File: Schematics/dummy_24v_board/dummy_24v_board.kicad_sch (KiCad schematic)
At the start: 2 parts, among them J1 Stack Male Edge Connector, J2 Conn_01x02_Socket

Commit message: Board setup with footprint
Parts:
- J2: footprint (none) -> footprints:CONN_2-1445057-2_TYCO
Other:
- moved on the sheet: J2
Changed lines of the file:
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@@
 	(symbol
 		(lib_id "Connector:Conn_01x02_Socket")
-		(at 90.17 62.23 0)
+		(at 85.09 71.12 0)
 		(unit 1)
 		(exclude_from_sim no)
@@
 		(on_board yes)
 		(dnp no)
-		(fields_autoplaced yes)
 		(property "Reference" "J2"
-			(at 91.44 62.2299 0)
+			(at 86.36 71.1199 0)
 			(effects
 				(font
@@
 		)
 		(property "Value" "Conn_01x02_Socket"
-			(at 91.44 64.7699 0)
+			(at 86.36 73.6599 0)
 			(effects
 				(font
@@
 			)
 		)
-		(property "Footprint" ""
-			(at 90.17 62.23 0)
+		(property "Footprint" "footprints:CONN_2-1445057-2_TYCO"
+			(at 89.154 64.516 0)
 			(effects
 				(font
 					(size 1.27 1.27)
 				)
-				(hide yes)
 			)
 		)
 		(property "Datasheet" "~"
-			(at 90.17 62.23 0)
+			(at 85.09 71.12 0)
 			(effects
 				(font
@@
 		)
 		(property "Description" "Generic connector, single row, 01x02, script generated"
-			(at 90.17 62.23 0)
+			(at 85.09 71.12 0)
 			(effects
 				(font

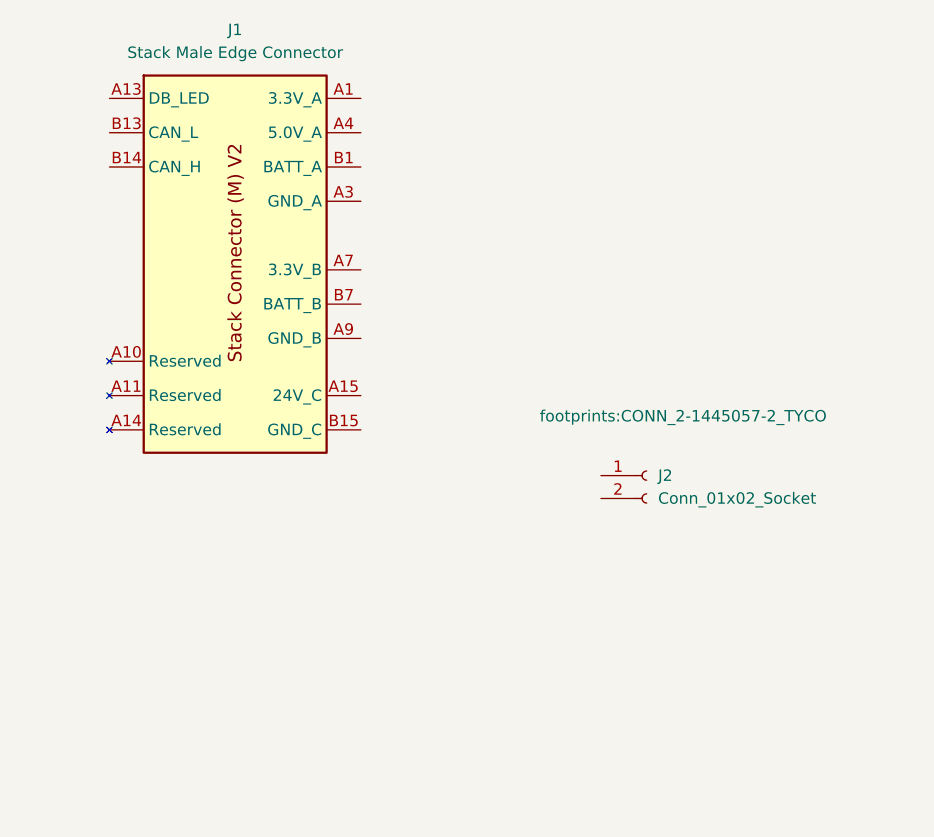
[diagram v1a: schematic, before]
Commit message: added two TestPoints for BATT 1&2
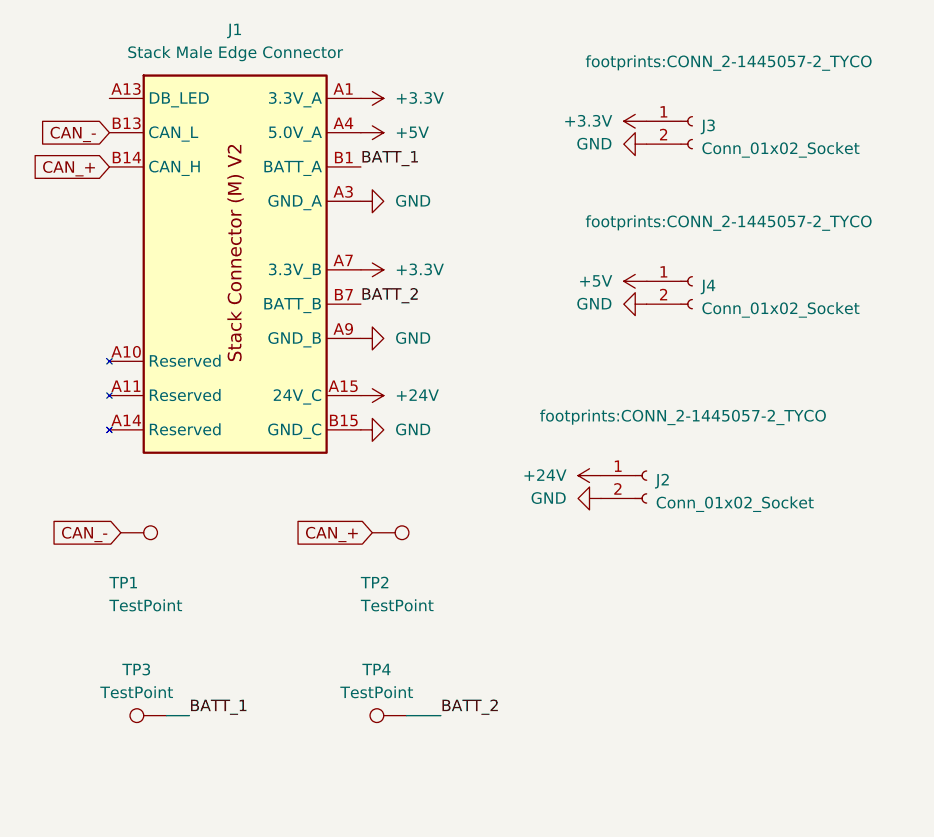
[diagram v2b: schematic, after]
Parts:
- added J3, J4: Conn_01x02_Socket, footprints:CONN_2-1445057-2_TYCO, symbol Connector:Conn_01x02_Socket
- added TP1, TP2, TP3, TP4: TestPoint, TestPoint:TestPoint_Pad_2.0x2.0mm, symbol Connector:TestPoint
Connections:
- net +3.3V: now reaches J1.A1 (3.3V_A), J1.A2 (3.3V_A)
- net +3.3V: now also J1.A7 (3.3V_B), J1.A8 (3.3V_B), J3.1 (Pin_1)
- net GND: now reaches J1.A12 (GND_B), J1.A9 (GND_B), J1.B10 (GND_B), J1.B11 (GND_B), J1.B12 (GND_B)
- net GND: now also J1.A3 (GND_A), J1.A6 (GND_A), J1.B15 (GND_C), J1.B16 (GND_C), J1.B17 (GND_C), J1.B18 (GND_C), J1.B4 (GND_A), J1.B5 (GND_A), J1.B6 (GND_A), J2.2 (Pin_2), J3.2 (Pin_2), J4.2 (Pin_2)
- net +24V: now reaches J1.A15 (24V_C), J1.A16 (24V_C), J1.A17 (24V_C), J1.A18 (24V_C)
- net +24V: now also J2.1 (Pin_1)
- net BATT_1: now reaches J1.B1 (BATT_A), J1.B2 (BATT_A), J1.B3 (BATT_A)
- net BATT_1: now also TP3.1
- net CAN_-: now reaches J1.B13 (CAN_L)
- net CAN_-: now also TP1.1
- net CAN_+: now reaches J1.B14 (CAN_H)
- net CAN_+: now also TP2.1
- net BATT_2: now reaches J1.B7 (BATT_B), J1.B8 (BATT_B), J1.B9 (BATT_B)
- net BATT_2: now also TP4.1
- net 5.0V_A renamed +5V
- net +5V: now also J4.1 (Pin_1)

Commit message: Connectors model added
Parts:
- J2, J3, J4: DIgiKey (none) -> 2-1445057-2
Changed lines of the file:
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@@
+			)
+		)
+		(property "DIgiKey" "2-1445057-2"
+			(at 90.17 31.75 0)
+			(effects
+				(font
+					(size 1.27 1.27)
+				)
+				(hide yes)
 			)
 		)
@@
 			)
 		)
+		(property "DIgiKey" "2-1445057-2"
+			(at 90.17 49.53 0)
+			(effects
+				(font
+					(size 1.27 1.27)
+				)
+				(hide yes)
+			)
+		)
 		(pin "2"
 		)
@@
 			)
 		)
+		(property "DIgiKey" ""
+			(at 39.37 48.26 0)
+			(effects
+				(font
+					(size 1.27 1.27)
+				)
+				(hide yes)
+			)
+		)
 		(pin "B6"
 		)
@@
 			)
 		)
+		(property "DIgiKey" ""
+			(at 54.61 77.47 0)
+			(effects
+				(font
+					(size 1.27 1.27)
+				)
+				(hide yes)
+			)
+		)
 		(pin "1"
 		)
@@
 			)
 		)
+		(property "DIgiKey" "2-1445057-2"
+			(at 85.09 71.12 0)
+			(effects
+				(font
+					(size 1.27 1.27)
+				)
+				(hide yes)
+			)
+		)
 		(pin "2"
 		)
@@
 		)
 		(property "Description" "test point"
+			(at 26.67 77.47 0)
+			(effects
+				(font
+					(size 1.27 1.27)
+				)
+				(hide yes)
+			)
+		)
+		(property "DIgiKey" ""
 			(at 26.67 77.47 0)
 			(effects
@@
 			)
 		)
+		(property "DIgiKey" ""
+			(at 58.42 97.79 0)
+			(effects
+				(font
+					(size 1.27 1.27)
+				)
+				(hide yes)
+			)
+		)
 		(pin "1"
 		)
@@
 			(at 31.75 97.79 0)
 			(effects
+				(font
+					(size 1.27 1.27)
+				)
+				(hide yes)
+			)
+		)
+		(property "DIgiKey" ""
+			(at 31.75 97.79 0)
+			(effects

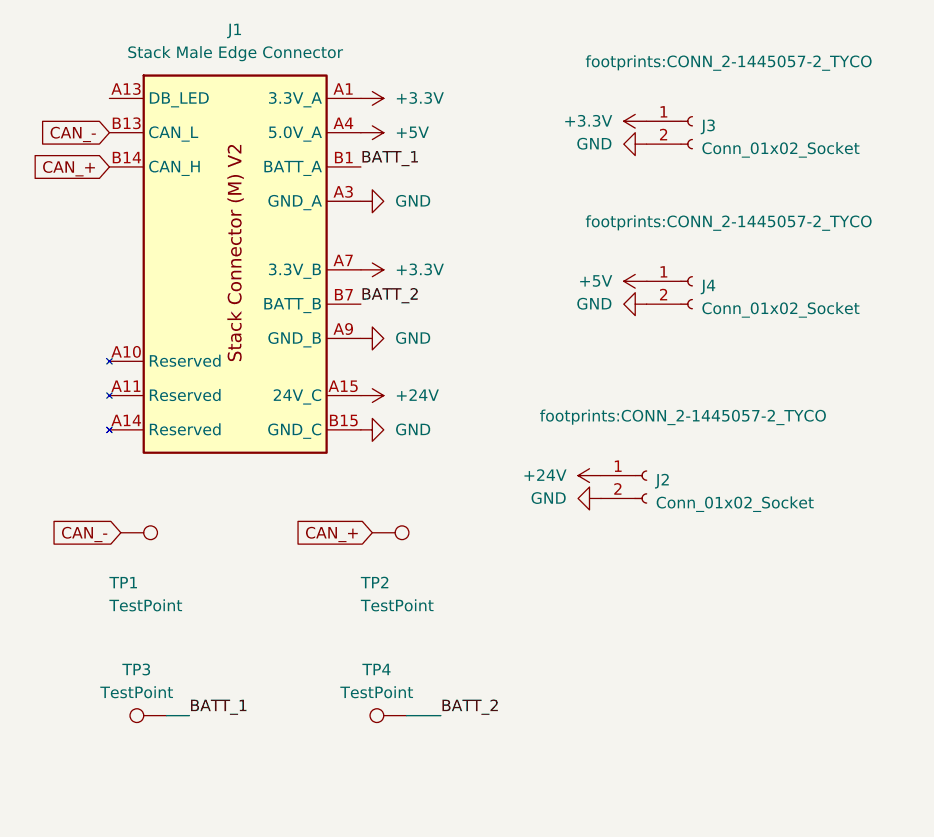
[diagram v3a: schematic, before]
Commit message: cleanup PCB, switch to solid copper pour, add GND tp, and updated silkscreen
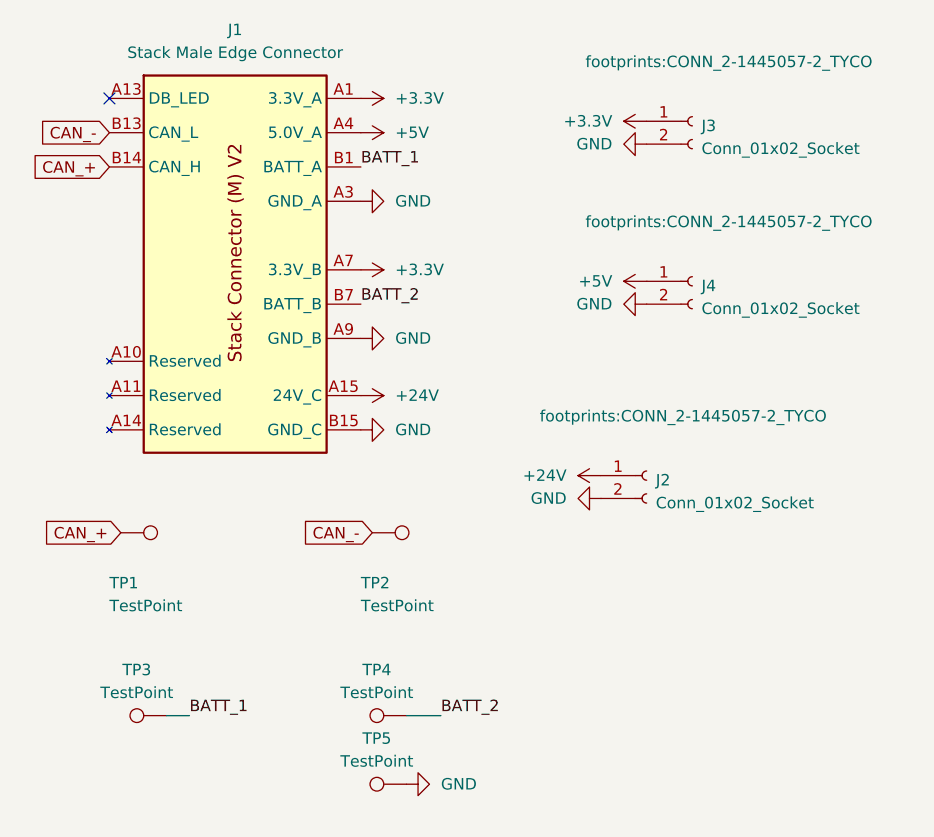
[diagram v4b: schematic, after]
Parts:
- added TP5: TestPoint, TestPoint:TestPoint_Pad_2.0x2.0mm, symbol Connector:TestPoint
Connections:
- net CAN_+: now also TP1.1; no longer TP2.1
- net CAN_-: now also TP2.1; no longer TP1.1
- net GND: now also TP5.1
- no-connect marks 0 -> 1
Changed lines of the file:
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@@
 	(generator_version "8.0")
 	(paper "A4")
+	(no_connect
+		(at 25.4 29.21)
+	)
 	(wire
 		(pts
@@
 	(label "BATT_1"
 		(at 34.29 97.79 0)
-		(fields_autoplaced yes)
 		(effects
 			(font
@@
 	(label "BATT_2"
 		(at 53.34 52.07 0)
-		(fields_autoplaced yes)
 		(effects
 			(font
@@
 	(label "BATT_1"
 		(at 53.34 36.83 0)
-		(fields_autoplaced yes)
 		(effects
 			(font
@@
 	(label "BATT_2"
 		(at 62.23 97.79 0)
-		(fields_autoplaced yes)
 		(effects
 			(font
@@
 		)
 	)
-	(global_label "CAN_+"
+	(global_label "CAN_-"
 		(shape input)
-		(at 54.61 77.47 180)
+		(at 25.4 33.02 180)
 		(fields_autoplaced yes)
 		(effects
@@
 		)
 		(property "Intersheetrefs" "${INTERSHEET_REFS}"
-			(at 45.3957 77.47 0)
+			(at 16.1857 33.02 0)
 			(effects
 				(font
@@
 	(global_label "CAN_-"
 		(shape input)
-		(at 25.4 33.02 180)
+		(at 54.61 77.47 180)
 		(fields_autoplaced yes)
 		(effects
@@
 		)
 		(property "Intersheetrefs" "${INTERSHEET_REFS}"
-			(at 16.1857 33.02 0)
+			(at 45.3957 77.47 0)
 			(effects
 				(font
@@
 		)
 	)
-	(global_label "CAN_-"
+	(global_label "CAN_+"
 		(shape input)
 		(at 26.67 77.47 180)
@@
 	)
 	(symbol
+		(lib_id "Connector:TestPoint")
+		(at 58.42 105.41 90)
+		(unit 1)
+		(exclude_from_sim no)
+		(in_bom yes)
+		(on_board yes)
+		(dnp no)
+		(fields_autoplaced yes)
+		(property "Reference" "TP5"
+			(at 55.118 100.33 90)
+			(effects
+				(font
+					(size 1.27 1.27)
+				)
+			)
+		)
+		(property "Value" "TestPoint"
+			(at 55.118 102.87 90)
+			(effects
+				(font
+					(size 1.27 1.27)
+				)
+			)
+		)
+		(property "Footprint" "TestPoint:TestPoint_Pad_2.0x2.0mm"
+			(at 58.42 100.33 0)
+			(effects
+				(font
+					(size 1.27 1.27)
+				)
+				(hide yes)
+			)
+		)
+		(property "Datasheet" "~"
+			(at 58.42 100.33 0)
+			(effects
+				(font
+					(size 1.27 1.27)
+				)
+				(hide yes)
+			)
+		)
+		(property "Description" "test point"
+			(at 58.42 105.41 0)
+			(effects
+				(font
+					(size 1.27 1.27)
+				)
+				(hide yes)
+			)
+		)
+		(property "DIgiKey" ""
+			(at 58.42 105.41 0)
+			(effects
+				(font
+					(size 1.27 1.27)
+				)
+				(hide yes)
+			)
+		)
+		(pin "1"
+		)
+		(instances
+			(project "dummy_24v_board"
+				(path "/f0325854-a423-47be-953e-4a5cbde51c3f"
+					(reference "TP5")
+					(unit 1)
+				)
+			)
+		)
+	)
+	(symbol
 		(lib_id "power:GND")
 		(at 53.34 55.88 90)
@@
 					(unit 1)
 				)
+			)
+		)
+	)
+	(symbol
+		(lib_id "power:GND")
+		(at 58.42 105.41 90)
+		(unit 1)
+		(exclude_from_sim no)
+		(in_bom yes)
+		(on_board yes)
+		(dnp no)
+		(fields_autoplaced yes)
+		(property "Reference" "#PWR14"
+			(at 64.77 105.41 0)
+			(effects
+				(font
+					(size 1.27 1.27)
+				)
+				(hide yes)
+			)
+		)
+		(property "Value" "GND"
+			(at 62.23 105.4099 90)
+			(effects
+				(font
+					(size 1.27 1.27)
+				)
+				(justify right)
+			)
+		)
+		(property "Footprint" ""
+			(at 58.42 105.41 0)
+			(effects
+				(font
+					(size 1.27 1.27)
+				)
+				(hide yes)
+			)
+		)
+		(property "Datasheet" ""
+			(at 58.42 105.41 0)
+			(effects
+				(font
+					(size 1.27 1.27)
+				)
+				(hide yes)
+			)
+		)
+		(property "Description" "Power symbol creates a global label with name \"GND\" , ground"
+			(at 58.42 105.41 0)
+			(effects
+				(font
+					(size 1.27 1.27)
+				)
+				(hide yes)
+			)
+		)
+		(pin "1"
+		)
+		(instances
+			(project "dummy_24v_board"
+				(path "/f0325854-a423-47be-953e-4a5cbde51c3f"
+					(reference "#PWR14")
+					(unit 1)
+				)

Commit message: updates to dummy board for splitting A and B power and new edge connector
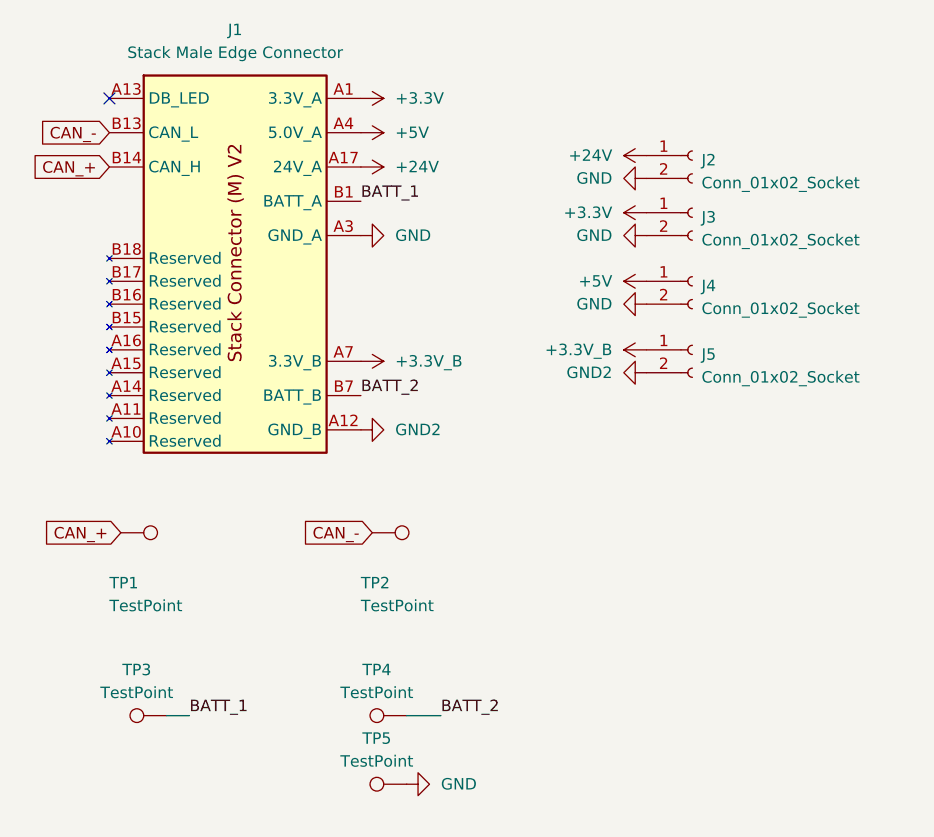
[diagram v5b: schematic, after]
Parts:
- removed J1: Stack Male Edge Connector, Connector_PCBEdge:BUS_PCIexpress_x1, symbol EdgeConnector:Stack Male Edge Connector
- added J1: Stack Male Edge Connector, Connector_PCBEdge:BUS_PCIexpress_x1, symbol EdgeConnectorV2:Stack Male Edge Connector
- added J5: Conn_01x02_Socket, footprints:CONN_2-1445057-2_TYCO, symbol Connector:Conn_01x02_Socket
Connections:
- net +24V: now also J1.A17 (24V_A), J1.A18 (24V_A)
- net +3.3V: now also J1.A1 (3.3V_A), J1.A2 (3.3V_A)
- net +5V: now also J1.A4 (5.0V_A), J1.A5 (5.0V_A)
- net BATT_1: now also J1.B1 (BATT_A), J1.B2 (BATT_A), J1.B3 (BATT_A)
- net BATT_2: now also J1.B7 (BATT_B), J1.B8 (BATT_B), J1.B9 (BATT_B)
- net CAN_+: now also J1.B14 (CAN_H)
- net CAN_-: now also J1.B13 (CAN_L)
- net GND: now also J1.A3 (GND_A), J1.A6 (GND_A), J1.B4 (GND_A), J1.B5 (GND_A), J1.B6 (GND_A)
- new net +3.3V_B: J1.A7 (3.3V_B), J1.A8 (3.3V_B), J5.1 (Pin_1)
- new net GND2: J1.A12 (GND_B), J1.A9 (GND_B), J1.B10 (GND_B), J1.B11 (GND_B), J1.B12 (GND_B), J5.2 (Pin_2)
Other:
- moved on the sheet: J2, J3

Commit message: Update dummy_24v_board.kicad_sch
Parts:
- added TP6: TestPoint, TestPoint:TestPoint_Pad_2.0x2.0mm, symbol Connector:TestPoint
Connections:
- net GND2: now also TP6.1
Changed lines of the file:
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@@
 	(label "BATT_1"
 		(at 34.29 97.79 0)
+		(fields_autoplaced yes)
 		(effects
 			(font
@@
 	(label "BATT_2"
 		(at 53.34 62.23 0)
+		(fields_autoplaced yes)
 		(effects
 			(font
@@
 	(label "BATT_1"
 		(at 53.34 40.64 0)
+		(fields_autoplaced yes)
 		(effects
 			(font
@@
 	(label "BATT_2"
 		(at 62.23 97.79 0)
+		(fields_autoplaced yes)
 		(effects
 			(font
@@
 	)
 	(symbol
+		(lib_id "power:GND")
+		(at 30.48 107.95 90)
+		(unit 1)
+		(exclude_from_sim no)
+		(in_bom yes)
+		(on_board yes)
+		(dnp no)
+		(fields_autoplaced yes)
+		(property "Reference" "#PWR016"
+			(at 36.83 107.95 0)
+			(effects
+				(font
+					(size 1.27 1.27)
+				)
+				(hide yes)
+			)
+		)
+		(property "Value" "GND2"
+			(at 34.29 107.9499 90)
+			(effects
+				(font
+					(size 1.27 1.27)
+				)
+				(justify right)
+			)
+		)
+		(property "Footprint" ""
+			(at 30.48 107.95 0)
+			(effects
+				(font
+					(size 1.27 1.27)
+				)
+				(hide yes)
+			)
+		)
+		(property "Datasheet" ""
+			(at 30.48 107.95 0)
+			(effects
+				(font
+					(size 1.27 1.27)
+				)
+				(hide yes)
+			)
+		)
+		(property "Description" "Power symbol creates a global label with name \"GND\" , ground"
+			(at 30.48 107.95 0)
+			(effects
+				(font
+					(size 1.27 1.27)
+				)
+				(hide yes)
+			)
+		)
+		(pin "1"
+		)
+		(instances
+			(project "dummy_24v_board"
+				(path "/f0325854-a423-47be-953e-4a5cbde51c3f"
+					(reference "#PWR016")
+					(unit 1)
+				)
+			)
+		)
+	)
+	(symbol
 		(lib_id "EdgeConnectorV2:Stack Male Edge Connector")
 		(at 39.37 48.26 0)
@@
 	)
 	(symbol
+		(lib_id "Connector:TestPoint")
+		(at 30.48 107.95 90)
+		(unit 1)
+		(exclude_from_sim no)
+		(in_bom yes)
+		(on_board yes)
+		(dnp no)
+		(fields_autoplaced yes)
+		(property "Reference" "TP6"
+			(at 27.178 102.87 90)
+			(effects
+				(font
+					(size 1.27 1.27)
+				)
+			)
+		)
+		(property "Value" "TestPoint"
+			(at 27.178 105.41 90)
+			(effects
+				(font
+					(size 1.27 1.27)
+				)
+			)
+		)
+		(property "Footprint" "TestPoint:TestPoint_Pad_2.0x2.0mm"
+			(at 30.48 102.87 0)
+			(effects
+				(font
+					(size 1.27 1.27)
+				)
+				(hide yes)
+			)
+		)
+		(property "Datasheet" "~"
+			(at 30.48 102.87 0)
+			(effects
+				(font
+					(size 1.27 1.27)
+				)
+				(hide yes)
+			)
+		)
+		(property "Description" "test point"
+			(at 30.48 107.95 0)
+			(effects
+				(font
+					(size 1.27 1.27)
+				)
+				(hide yes)
+			)
+		)
+		(property "DIgiKey" ""
+			(at 30.48 107.95 0)
+			(effects
+				(font
+					(size 1.27 1.27)
+				)
+				(hide yes)
+			)
+		)
+		(pin "1"
+		)
+		(instances
+			(project "dummy_24v_board"
+				(path "/f0325854-a423-47be-953e-4a5cbde51c3f"
+					(reference "TP6")
+					(unit 1)
+				)
+			)
+		)
+	)
+	(symbol
 		(lib_id "Connector:Conn_01x02_Socket")
 		(at 90.17 49.53 0)
@@
 		(dnp no)
 		(fields_autoplaced yes)
-		(property "Reference" "#PWR12"
+		(property "Reference" "#PWR012"
 			(at 88.9 57.15 0)
 			(effects
@@
 			(project "dummy_24v_board"
 				(path "/f0325854-a423-47be-953e-4a5cbde51c3f"
-					(reference "#PWR12")
+					(reference "#PWR012")
 					(unit 1)
 				)
@@
 		(dnp no)
 		(fields_autoplaced yes)
-		(property "Reference" "#PWR1"
+		(property "Reference" "#PWR01"
 			(at 49.53 36.83 0)
 			(effects
@@
 			(project "dummy_24v_board"
 				(path "/f0325854-a423-47be-953e-4a5cbde51c3f"
-					(reference "#PWR1")
+					(reference "#PWR01")
 					(unit 1)
 				)
@@
 		(dnp no)
 		(fields_autoplaced yes)
-		(property "Reference" "#PWR15"
+		(property "Reference" "#PWR015"
 			(at 78.74 59.69 0)
 			(effects
@@
 			(project "dummy_24v_board"
 				(path "/f0325854-a423-47be-953e-4a5cbde51c3f"
-					(reference "#PWR15")
+					(reference "#PWR015")
 					(unit 1)
 				)
@@
 		(dnp no)
 		(fields_autoplaced yes)
-		(property "Reference" "#PWR14"
+		(property "Reference" "#PWR014"
 			(at 64.77 105.41 0)
 			(effects
@@
 			(project "dummy_24v_board"
 				(path "/f0325854-a423-47be-953e-4a5cbde51c3f"
-					(reference "#PWR14")
+					(reference "#PWR014")
 					(unit 1)
 				)
@@
 		(dnp no)
 		(fields_autoplaced yes)
-		(property "Reference" "#PWR11"
+		(property "Reference" "#PWR011"
 			(at 59.69 44.45 0)
 			(effects
@@
 			(project "dummy_24v_board"
 				(path "/f0325854-a423-47be-953e-4a5cbde51c3f"
-					(reference "#PWR11")
+					(reference "#PWR011")
 					(unit 1)
 				)
@@
 		(dnp no)
 		(fields_autoplaced yes)
-		(property "Reference" "#PWR6"
+		(property "Reference" "#PWR06"
 			(at 49.53 33.02 0)
 			(effects
@@
 			(project "dummy_24v_board"
 				(path "/f0325854-a423-47be-953e-4a5cbde51c3f"
-					(reference "#PWR6")
-					(unit 1)
-				)
+					(reference "#PWR06")
+					(unit 1)
+				)
